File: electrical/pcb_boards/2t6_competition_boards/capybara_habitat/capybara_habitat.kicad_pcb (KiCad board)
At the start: 2 copper layers, 92 parts, among them J10 leds_sw, J11 leds_power, J12 2nd_disp_sw, J13 spare_usb_2nd_disp_pwr, J14 aud_sig_out_a, J15 aud_sig_out_b, J16 aud_sig_in, J18 spkrs_sw, J2 charger_buck_in, J3 vbatt, J5 Raspberry_Pi_4, J7 1st_disp_sw, J8 leds_power, J9 monitor_power, U1 Adafruit_INA219, U2 Adafruit_INA219, U3 LTC3114IFE-1_TRPBF, U4 LT8610ABEMSE-5-TRPBF, U5 TPS22810DBV, U6 TPS22810DBV, U7 TPS22810DBV, U8 TPS22810DBV, U9 PAM8406D

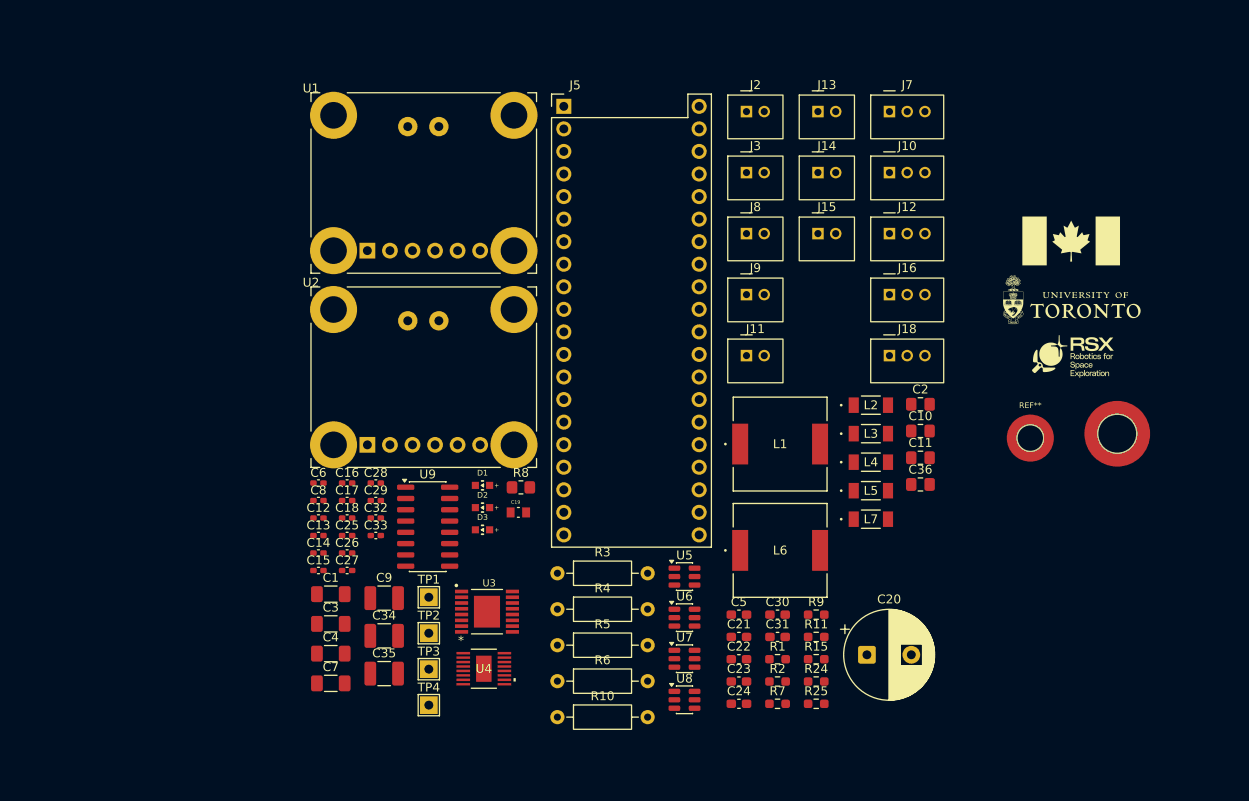
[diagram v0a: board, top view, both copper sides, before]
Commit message: Female DC Barrel Jack footprint added
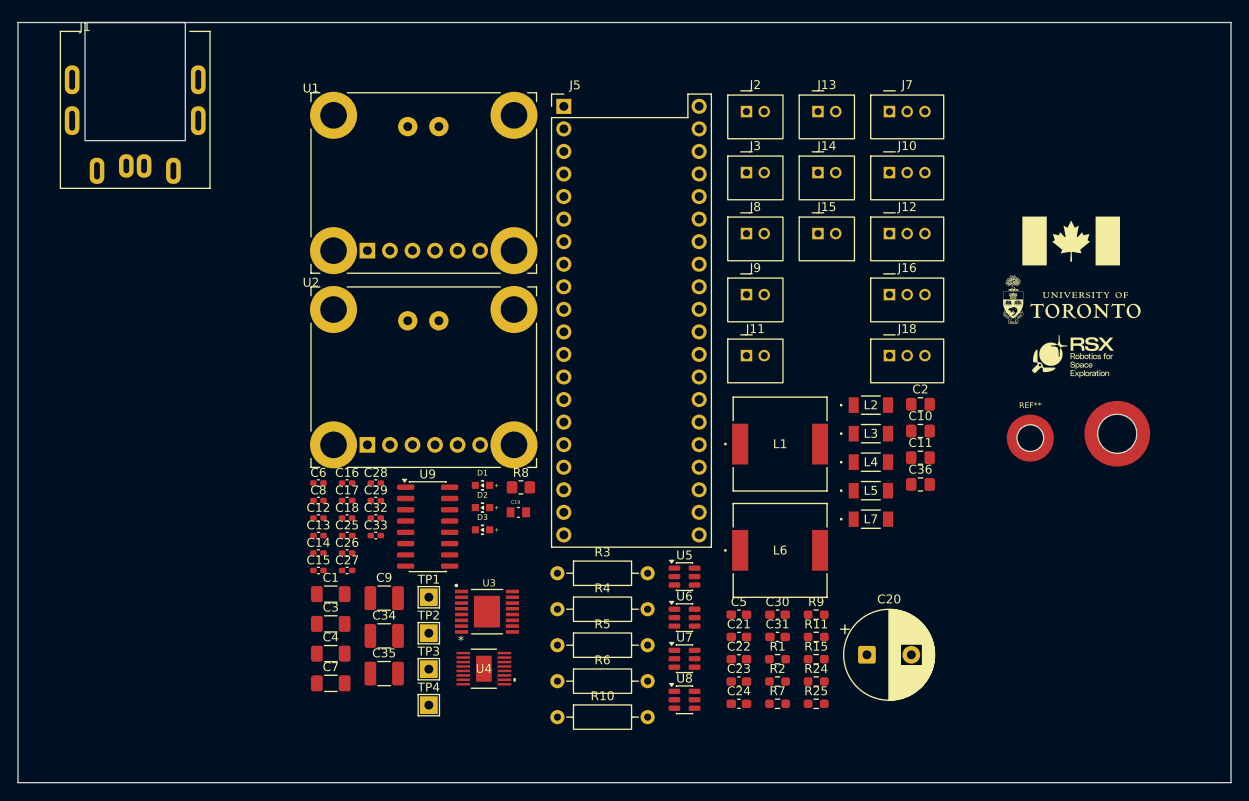
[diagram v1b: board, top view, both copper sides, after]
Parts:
- added J1: Barrel_Jack, RSX_CanSat_Custom_KiCad_Footprints:Female_DC_Power_Barrel_Jack, F.Cu at (84.8, 53.0)
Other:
- board outline added: 136.6 x 85.6 mm

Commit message: working on gnd station pcb
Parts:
- removed the REF** at (191.2, 98.8)
- removed the REF** at (201.0, 98.4)
- added J4: Raspberry_Pi_4, Connector_PinHeader_2.54mm:PinHeader_2x20_P2.54mm_Vertical, F.Cu at (57.0, 78.8)
- added R12: 100, Resistor_SMD:R_0603_1608Metric_Pad0.98x0.95mm_HandSolder, F.Cu at (102.4, 124.5)
- added R13: 100, Resistor_SMD:R_0603_1608Metric_Pad0.98x0.95mm_HandSolder, F.Cu at (102.4, 127.0)
- added R14: 100, Resistor_SMD:R_0603_1608Metric_Pad0.98x0.95mm_HandSolder, F.Cu at (102.4, 129.5)
- added R16: 100, Resistor_SMD:R_0603_1608Metric_Pad0.98x0.95mm_HandSolder, F.Cu at (102.4, 132.0)
- added REF**: WA-SMSI_9774030360, RSX_CanSat_Custom_KiCad_Footprints:WA-SMSI_9774030360, B.Cu at (53.5, 72.9)
- added REF**: WA-SMSI_9774030360, RSX_CanSat_Custom_KiCad_Footprints:WA-SMSI_9774030360, B.Cu at (243.5, 132.9)
- added REF**: WA-SMSI_9774030360, RSX_CanSat_Custom_KiCad_Footprints:WA-SMSI_9774030360, B.Cu at (243.5, 72.9)
- added REF**: WA-SMSI_9774030360, RSX_CanSat_Custom_KiCad_Footprints:WA-SMSI_9774030360, B.Cu at (53.5, 132.9)
- J11: value leds_power -> monitor2_power
- J9: value monitor_power -> monitor1_power
- moved J1 172.9 mm to (233.7, 140.8), turned to 180 degrees
- moved G*** 143.2 mm to (80.7, 161.8)
- moved G*** 143.2 mm to (80.7, 168.6)
- moved G*** 143.2 mm to (80.9, 174.8)
- moved C2 123.3 mm to (78.0, 166.0), turned to -90 degrees
- moved U2 113.1 mm to (221.6, 101.2)
- moved U1 113.1 mm to (221.6, 79.1)
- moved L3 106.4 mm to (79.8, 47.4)
- moved R9 99.4 mm to (68.4, 130.5)
- moved R7 98.4 mm to (64.3, 130.5)
- moved L1 96.6 mm to (85.0, 156.5), turned to 180 degrees
- moved R2 95.3 mm to (78.0, 169.9), turned to 90 degrees
- moved R15 94.9 mm to (72.4, 130.5)
- moved R8 93.6 mm to (78.0, 179.5)
- moved C5 93.5 mm to (86.5, 178.5)
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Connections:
- J11 pad 1: Net-(U8-QOD) -> Net-(U8-VOUT)
- J12 pad 1: pi_leds -> pi_2nd_disp
- J5 pad 1: unconnected-(J5-3V3-Pad1) -> Net-(J4-3V3-Pad1)
- J5 pad 10: unconnected-(J5-GPIO15/UART_RXD-Pad10) -> Net-(J4-GPIO15/UART_RXD)
- J5 pad 11: unconnected-(J5-GPIO17/SPI1_~{CE1}-Pad11) -> Net-(J4-GPIO17/SPI1_~{CE1})
- J5 pad 12: unconnected-(J5-GPIO18/SPI1_~{CE0}/PCM_CLK/PWM0-Pad12) -> Net-(J4-GPIO18/SPI1_~{CE0}/PCM_CLK/PWM0)
- J5 pad 15: unconnected-(J5-GPIO22/SDIO_CLK-Pad15) -> Net-(J4-GPIO22/SDIO_CLK)
- J5 pad 16: unconnected-(J5-GPIO23/SDIO_CMD-Pad16) -> Net-(J4-GPIO23/SDIO_CMD)
- J5 pad 17: unconnected-(J5-3V3-Pad1)_1 -> Net-(J4-3V3-Pad1)
- J5 pad 19: unconnected-(J5-MOSI_SPI0/GPIO10-Pad19) -> Net-(J4-MOSI_SPI0/GPIO10)
- J5 pad 21: unconnected-(J5-MISO_SPI0/GPIO09-Pad21) -> Net-(J4-MISO_SPI0/GPIO09)
- J5 pad 23: unconnected-(J5-SCLK_SPI0/GPIO11-Pad23) -> Net-(J4-SCLK_SPI0/GPIO11)
- J5 pad 24: unconnected-(J5-~{CE0}_SPI0/GPIO08-Pad24) -> Net-(J4-~{CE0}_SPI0/GPIO08)
- J5 pad 26: unconnected-(J5-~{CE1}_SPI0/GPIO07-Pad26) -> Net-(J4-~{CE1}_SPI0/GPIO07)
- J5 pad 27: unconnected-(J5-ID_SD_I2C0/GPIO00-Pad27) -> Net-(J4-ID_SD_I2C0/GPIO00)
- J5 pad 28: unconnected-(J5-ID_SC_I2C0/GPIO01-Pad28) -> Net-(J4-ID_SC_I2C0/GPIO01)
- J5 pad 29: unconnected-(J5-GPCLK1/GPIO05-Pad29) -> Net-(J4-GPCLK1/GPIO05)
- J5 pad 31: unconnected-(J5-GPCLK2/GPIO06-Pad31) -> Net-(J4-GPCLK2/GPIO06)
- J5 pad 32: unconnected-(J5-GPIO12/PWM0-Pad32) -> Net-(J4-GPIO12/PWM0)
- J5 pad 33: unconnected-(J5-GPIO13/PWM1-Pad33) -> Net-(J4-GPIO13/PWM1)
- J5 pad 35: unconnected-(J5-GPIO19/SPI1_MISO/PCM_FS-Pad35) -> Net-(J4-GPIO19/SPI1_MISO/PCM_FS)
- J5 pad 36: unconnected-(J5-GPIO16/SPI1_~{CE2}-Pad36) -> Net-(J4-GPIO16/SPI1_~{CE2})
- J5 pad 38: unconnected-(J5-GPIO20/SPI1_MOSI/PCM_DIN/PWM1-Pad38) -> Net-(J4-GPIO20/SPI1_MOSI/PCM_DIN/PWM1)
- J5 pad 40: unconnected-(J5-GPIO21/SPI1_SCLK/PCM_DOUT-Pad40) -> Net-(J4-GPIO21/SPI1_SCLK/PCM_DOUT)
- J5 pad 7: unconnected-(J5-GPCLK0/GPIO04-Pad7) -> Net-(J4-GPCLK0/GPIO04)
- J5 pad 8: unconnected-(J5-GPIO14/UART_TXD-Pad8) -> Net-(J4-GPIO14/UART_TXD)
- J8 pad 1: Net-(U6-QOD) -> Net-(U6-VOUT)
- J9 pad 1: Net-(U7-QOD) -> Net-(U7-VOUT)
- U5 pad 5: aud_control -> Net-(U5-QOD)
- U6 pad 6: Net-(U6-QOD) -> Net-(U6-VOUT)
- U7 pad 6: Net-(U7-QOD) -> Net-(U7-VOUT)
- U8 pad 6: Net-(U8-QOD) -> Net-(U8-VOUT)
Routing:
- net GND: track 0.00 -> 21.5 mm
- net 12.0v: track 0.00 -> 2.88 mm
- net 16.8v: track 0.00 -> 2.87 mm
- net 5.0v: track 0.00 -> 2.84 mm
- net Net-(D2-A): track 0.00 -> 2.00 mm
- net Net-(D1-A): track 0.00 -> 1.84 mm
- net Net-(D3-A): track 0.00 -> 1.75 mm
- added copper zone on B.Cu, net GND
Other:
- board size 136.6 x 85.6 mm -> 200 x 70 mm

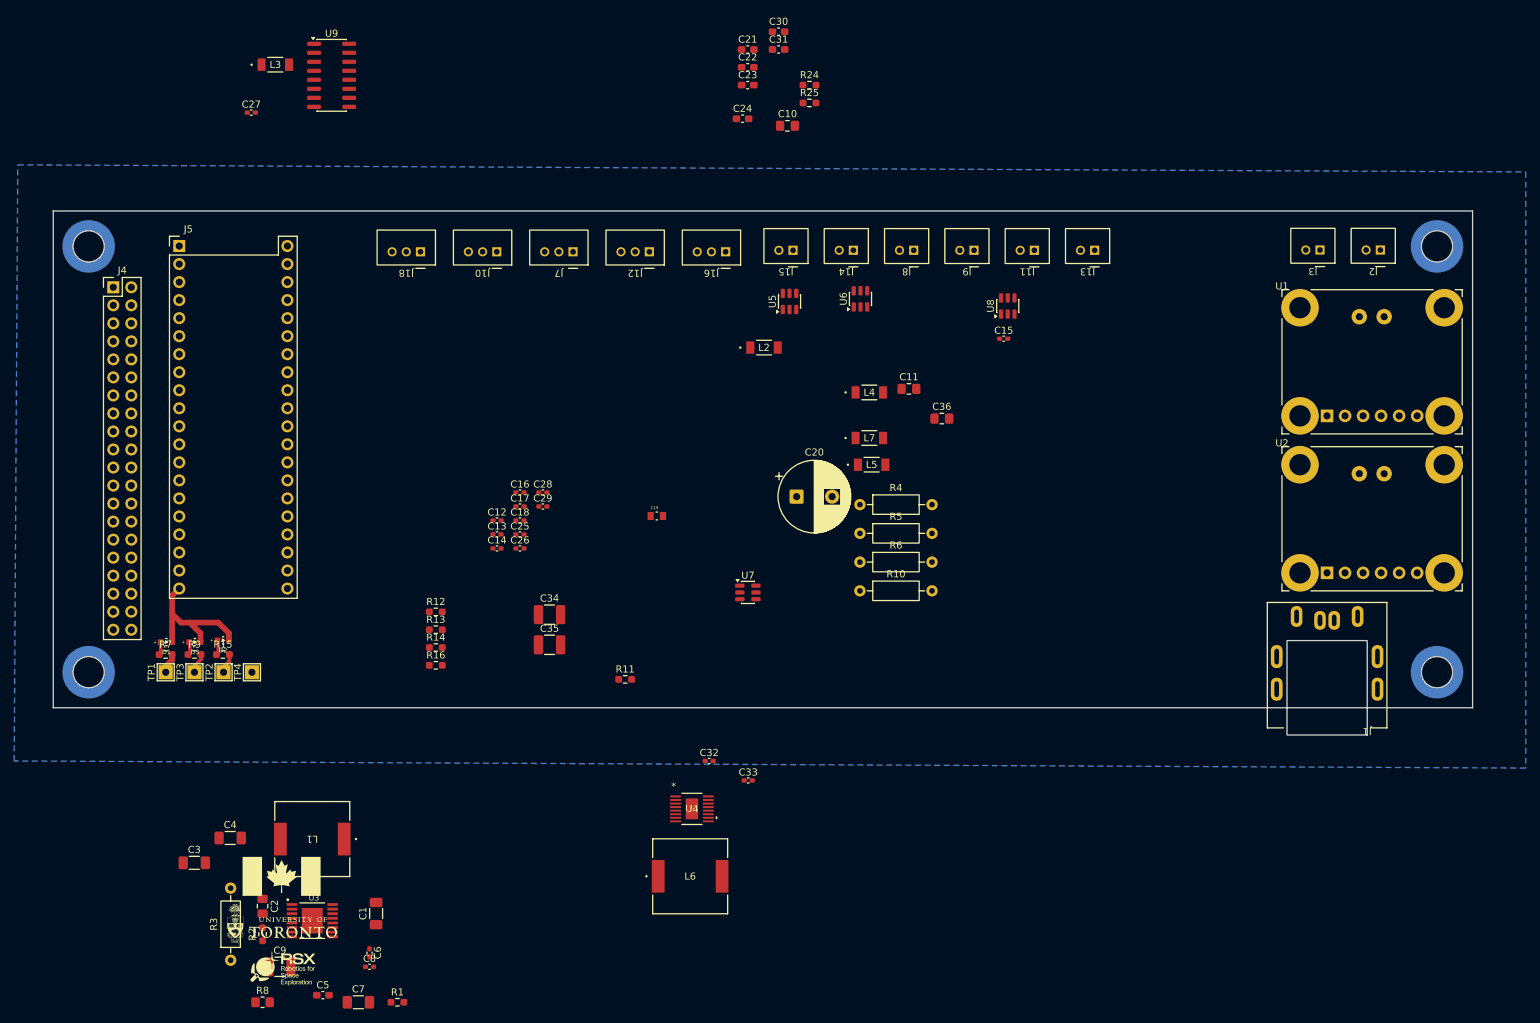
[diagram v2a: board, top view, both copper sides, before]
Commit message: gnd station schematic bulk complete, need to fix DRC and JST connections
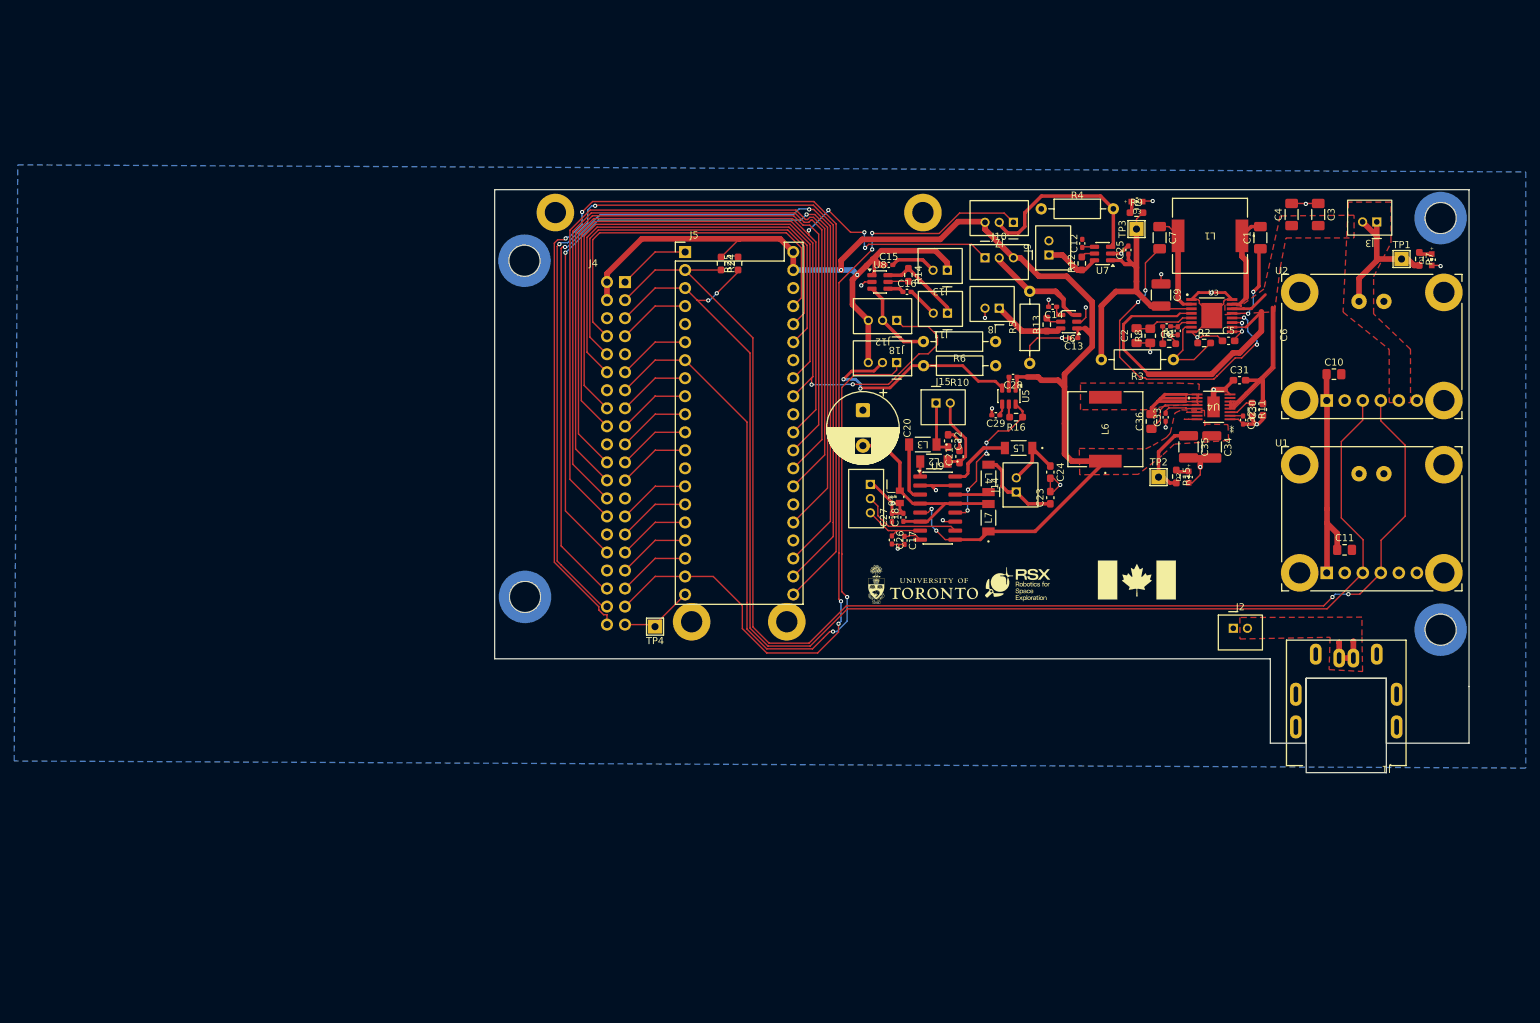
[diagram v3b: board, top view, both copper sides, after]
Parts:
- J4: footprint Connector_PinHeader_2.54mm:PinHeader_2x20_P2.54mm_Vertical -> RSX_CanSat_Custom_KiCad_Footprints:Reverse_Connector_PinHeader_2.54mmPinHeader_2x20_P2.54mm_Vertical
- moved D1 186.3 mm to (242.7, 74.9), turned to 90 degrees
- moved R7 185.2 mm to (241.0, 74.8), turned to -90 degrees
- moved TP1 183.6 mm to (238.5, 74.8), turned to 0 degrees
- moved C3 182.8 mm to (226.8, 68.5), turned to -90 degrees
- moved C4 173.5 mm to (223.0, 68.5), turned to 90 degrees
- moved R3 157.5 mm to (206.3, 88.9), turned to 180 degrees
- moved C5 157.4 mm to (214.1, 86.3)
- moved C1 156.8 mm to (218.6, 71.8)
- moved R2 156.7 mm to (210.7, 86.6), turned to 0 degrees
- moved R8 156.4 mm to (203.1, 85.6), turned to 90 degrees
- moved C9 156.1 mm to (204.6, 79.8), turned to -90 degrees
- moved C7 156.1 mm to (204.4, 71.8), turned to -90 degrees
- moved U3 152.8 mm to (211.8, 82.8)
- moved L1 152.4 mm to (211.5, 71.5)
- moved C2 147.1 mm to (201.2, 85.6), turned to 90 degrees
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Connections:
- U2 pad 5: unconnected-(U2-PadVIN-)_1 -> 16.8v
- U2 pad VIN-: unconnected-(U2-PadVIN-) -> 16.8v
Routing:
- net 5.0v: track 2.84 -> 255.0 mm, vias 0 -> 4
- net SDA: track 0.00 -> 190.2 mm, vias 0 -> 2
- net SCL: track 0.00 -> 188.6 mm, vias 0 -> 2
- net Net-(J4-GPIO21/SPI1_SCLK/PCM_DOUT): track 0.00 -> 156.3 mm, vias 0 -> 2
- net Net-(J4-GPIO20/SPI1_MOSI/PCM_DIN/PWM1): track 0.00 -> 149.4 mm, vias 0 -> 2
- net Net-(J4-GPIO16/SPI1_~{CE2}): track 0.00 -> 141.1 mm, vias 0 -> 2
- net pi_leds: track 0.00 -> 128.8 mm, vias 0 -> 4
- net Net-(J4-GPIO12/PWM0): track 0.00 -> 128.2 mm, vias 0 -> 2
- net pi_1st_disp: track 0.00 -> 119.5 mm, vias 0 -> 4
- net Net-(J4-ID_SC_I2C0/GPIO01): track 0.00 -> 119.1 mm
- net pi_2nd_disp: track 0.00 -> 115.0 mm, vias 0 -> 2
- net 16.8v: track 2.87 -> 117.4 mm
- net Net-(J4-~{CE1}_SPI0/GPIO07): track 0.00 -> 112.3 mm
- net GND: track 21.5 -> 133.4 mm, vias 0 -> 25
- net pi_spkrs: track 0.00 -> 111.7 mm, vias 0 -> 2
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- added copper zone on F.Cu, net 16.8v
- added copper zone on F.Cu, net 5.0v
- added copper zone on F.Cu, net Net-(C36-Pad2)
- added copper zone on F.Cu, net Net-(J1-Pad1)
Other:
- board size 200 x 70 mm -> 137.3 x 78 mm
- board text added: "${REFERENCE}"

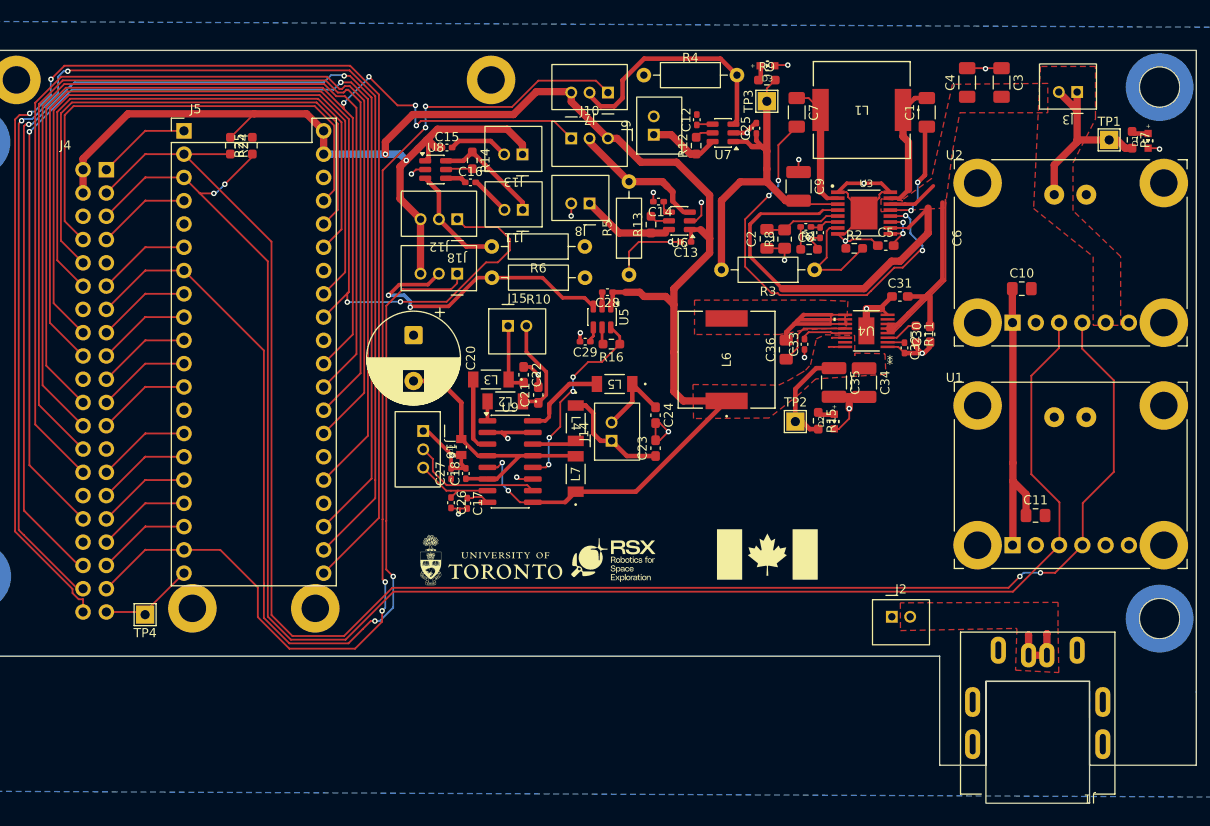
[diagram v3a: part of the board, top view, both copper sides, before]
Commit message: Initial ERC fixes for ground station board
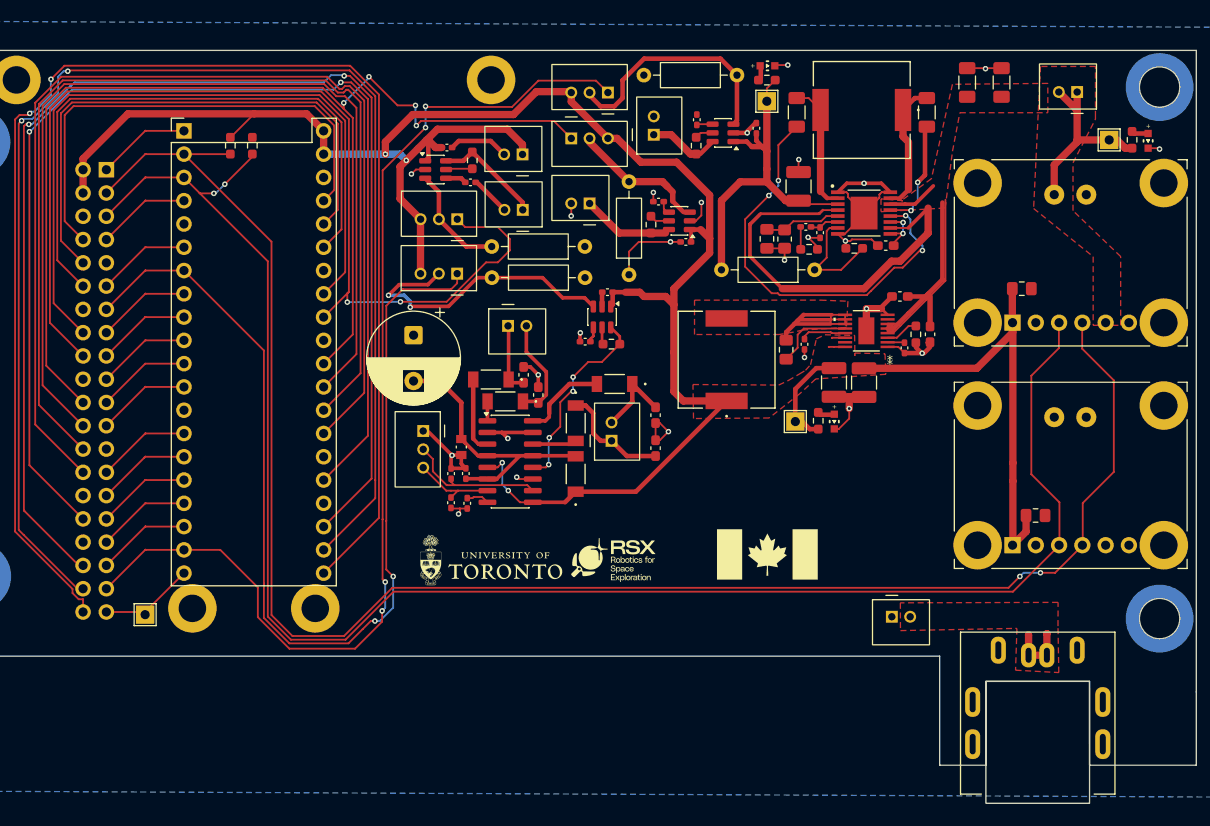
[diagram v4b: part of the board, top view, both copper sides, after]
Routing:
- net 5.0v: track 255.0 -> 273.4 mm
